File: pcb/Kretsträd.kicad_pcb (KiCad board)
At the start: 2 copper layers, 112.8 x 95.2 mm, 52 parts, among them J1 Conn_01x02_Female, J2 Conn_01x02_Female, J3 Conn_01x02_Female, J4 Conn_01x02_Female, SW1 SW_PUSH, SW10 SW_PUSH, SW11 SW_PUSH, SW12 SW_PUSH, SW13 SW_PUSH, SW14 SW_PUSH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

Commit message: Minor changes here and there.
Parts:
- moved PWR_SW_1 0.20 mm to (186.3, 125.1)
- moved PWR_SW_2 0.20 mm to (186.3, 125.1)
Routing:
- net BT+: track 58.4 -> 56.3 mm
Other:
- outline, holes or cut-outs redrawn

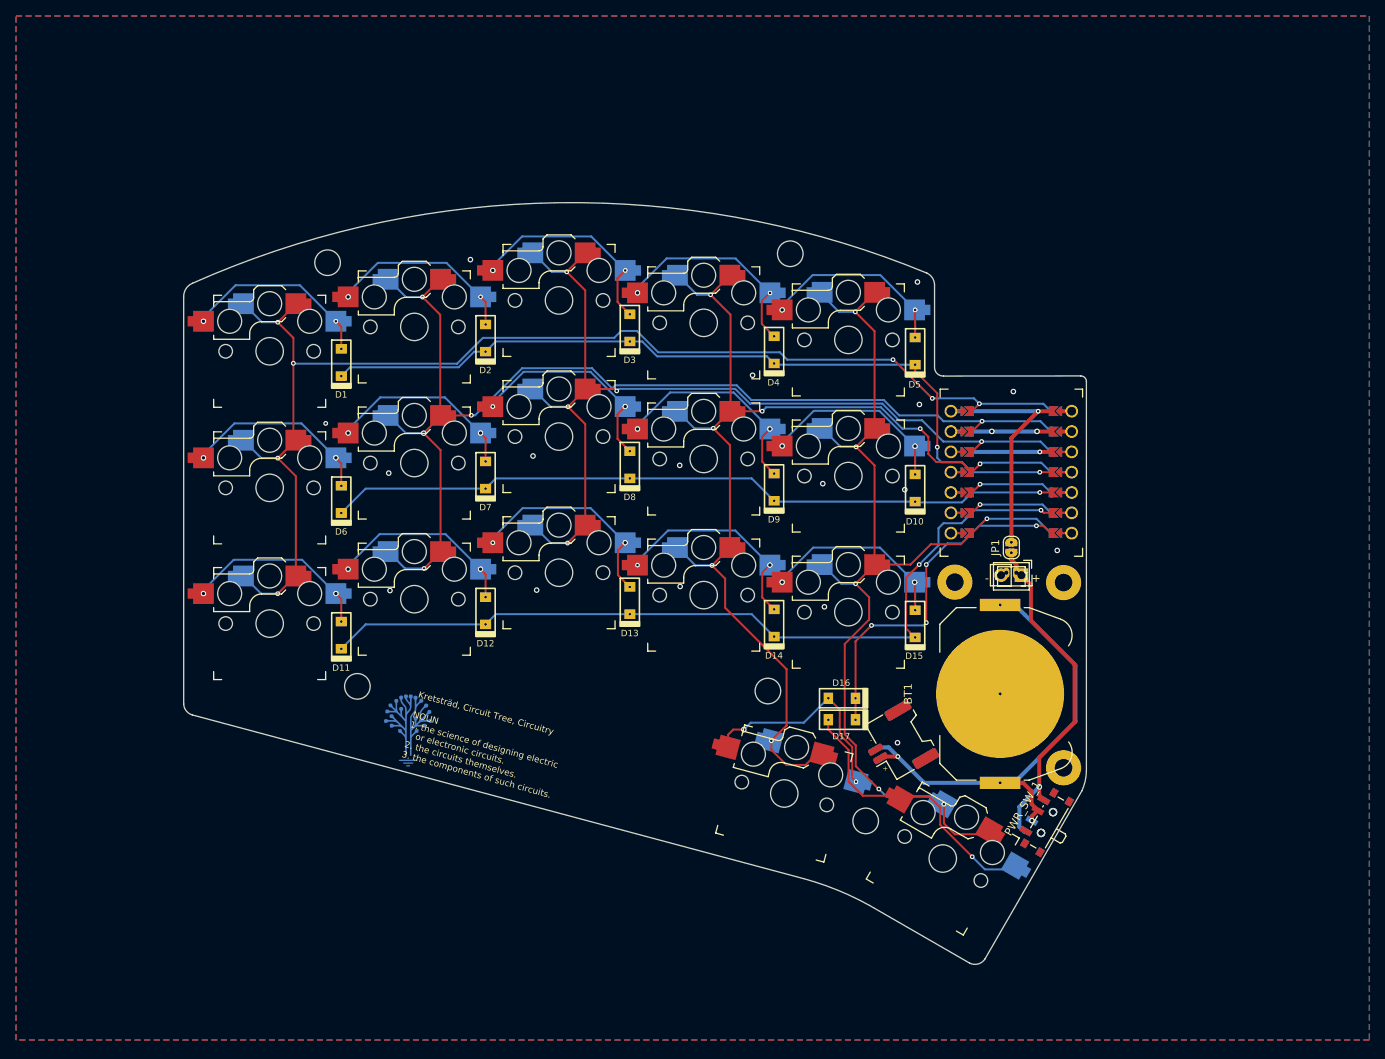
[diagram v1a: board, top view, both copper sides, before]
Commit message: 1. Moved down col0 and col1 (out-most columns). 2. Rerouted alot to avoid 'dead zones'. 3. Added tear drops for the same reason. 4. Minor change to edge shape. 5. Other minor changes.
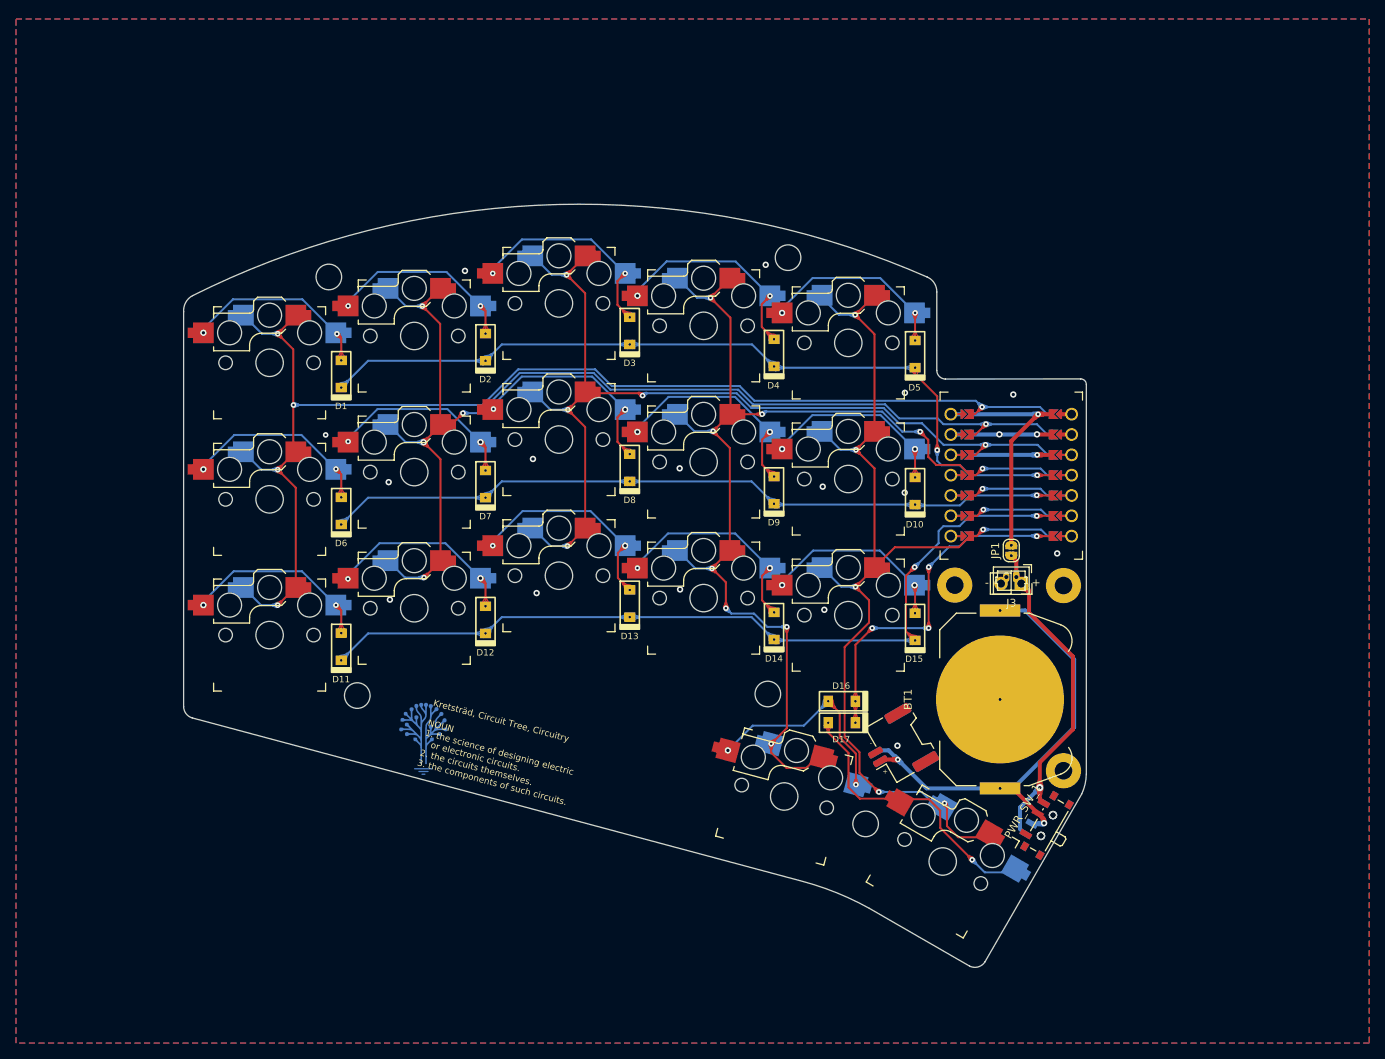
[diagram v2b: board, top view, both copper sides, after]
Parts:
- moved G*** 2.18 mm to (108.4, 113.7)
- moved TH1 1.79 mm to (96.8, 57.1)
- moved D1 1.44 mm to (98.4, 69.2)
- moved D11 1.44 mm to (98.4, 103.3)
- moved SW11 1.44 mm to (89.4, 101.8)
- moved D6 1.44 mm to (98.4, 86.3)
- moved SW1 1.44 mm to (89.4, 67.8)
- moved SW6 1.44 mm to (89.4, 84.9)
- moved TH3 1.15 mm to (100.4, 109.4)
- moved SW2 1.13 mm to (107.5, 64.4)
- moved D12 1.13 mm to (116.4, 99.9)
- moved D2 1.13 mm to (116.4, 65.8)
- moved D7 1.13 mm to (116.4, 82.9)
- moved SW12 1.13 mm to (107.5, 98.5)
- moved SW7 1.13 mm to (107.5, 81.4)
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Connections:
- SW10 pad : (no net) -> col4
- SW14 pad : (no net) -> col3
- SW15 pad : (no net) -> col4
- SW16 pad : (no net) -> col3
- SW17 pad : (no net) -> col4
- SW4 pad : (no net) -> col3
- SW5 pad : (no net) -> col4
- SW9 pad : (no net) -> col3
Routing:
- net col3: track 135.0 -> 137.3 mm, vias 7 -> 9
- net BT+: track 56.3 -> 57.8 mm
- net col0: track 156.2 -> 154.8 mm, vias 7 -> 5
- net col1: track 138.9 -> 137.9 mm
- net Net-(D16-Pad2): track 27.9 -> 26.9 mm
- net /PWR: track 42.7 -> 42.0 mm
- net row3: track 44.8 -> 44.3 mm
- net GND: vias 19 -> 18
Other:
- board size 112.8 x 95.2 mm -> 112.8 x 95.4 mm

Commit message: No comment.
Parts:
- moved D11 0.72 mm to (97.7, 103.1)
- moved D6 0.72 mm to (97.7, 86.2)
- moved D1 0.71 mm to (97.7, 69.1)
- moved D3 0.69 mm to (133.9, 64.1)
- moved D7 0.68 mm to (115.8, 82.7)
- moved D12 0.67 mm to (115.8, 99.8)
- moved D13 0.66 mm to (133.9, 98.2)
- moved D2 0.66 mm to (115.8, 65.7)
- moved D9 0.66 mm to (151.9, 83.3)
- moved D8 0.65 mm to (133.9, 81.1)
- moved D14 0.63 mm to (151.9, 100.4)
- moved D4 0.59 mm to (151.9, 66.3)
- moved D10 0.22 mm to (170.0, 83.6)
- moved D15 0.18 mm to (170.0, 100.6)
- moved D5 0.14 mm to (170.0, 66.6)
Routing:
- net row1: track 92.2 -> 94.0 mm
- net row0: track 102.7 -> 103.5 mm
- net Net-(D4-Pad2): track 27.0 -> 26.3 mm
- net Net-(D14-Pad2): track 27.0 -> 26.4 mm
- net Net-(D12-Pad2): track 24.3 -> 23.7 mm
- net Net-(D9-Pad2): track 27.1 -> 26.5 mm
- net row2: track 105.4 -> 104.9 mm
- net row3: track 44.3 -> 43.9 mm, vias 4 -> 2
